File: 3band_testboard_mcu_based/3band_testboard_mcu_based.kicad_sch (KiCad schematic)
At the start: 0 parts

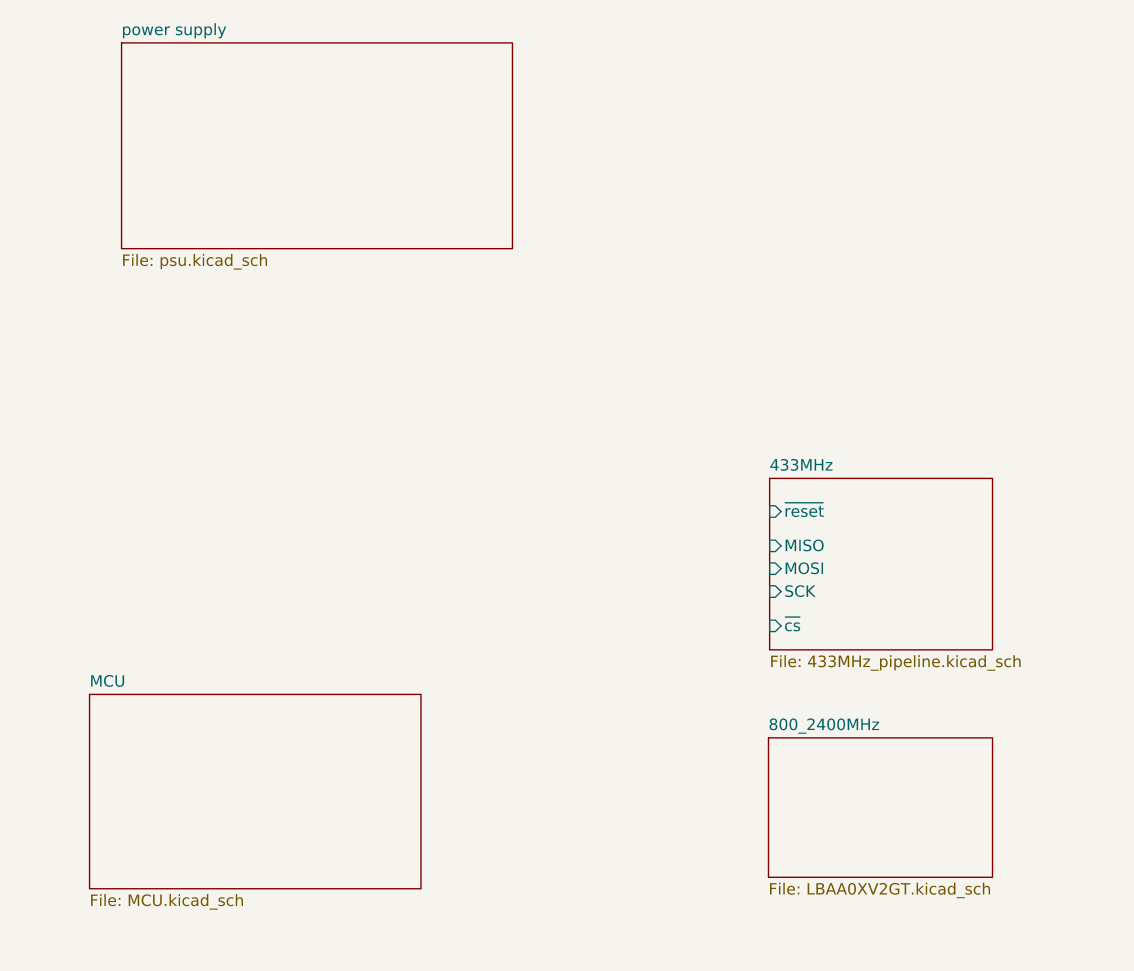
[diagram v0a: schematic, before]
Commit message: Færdiggjorde GPIO
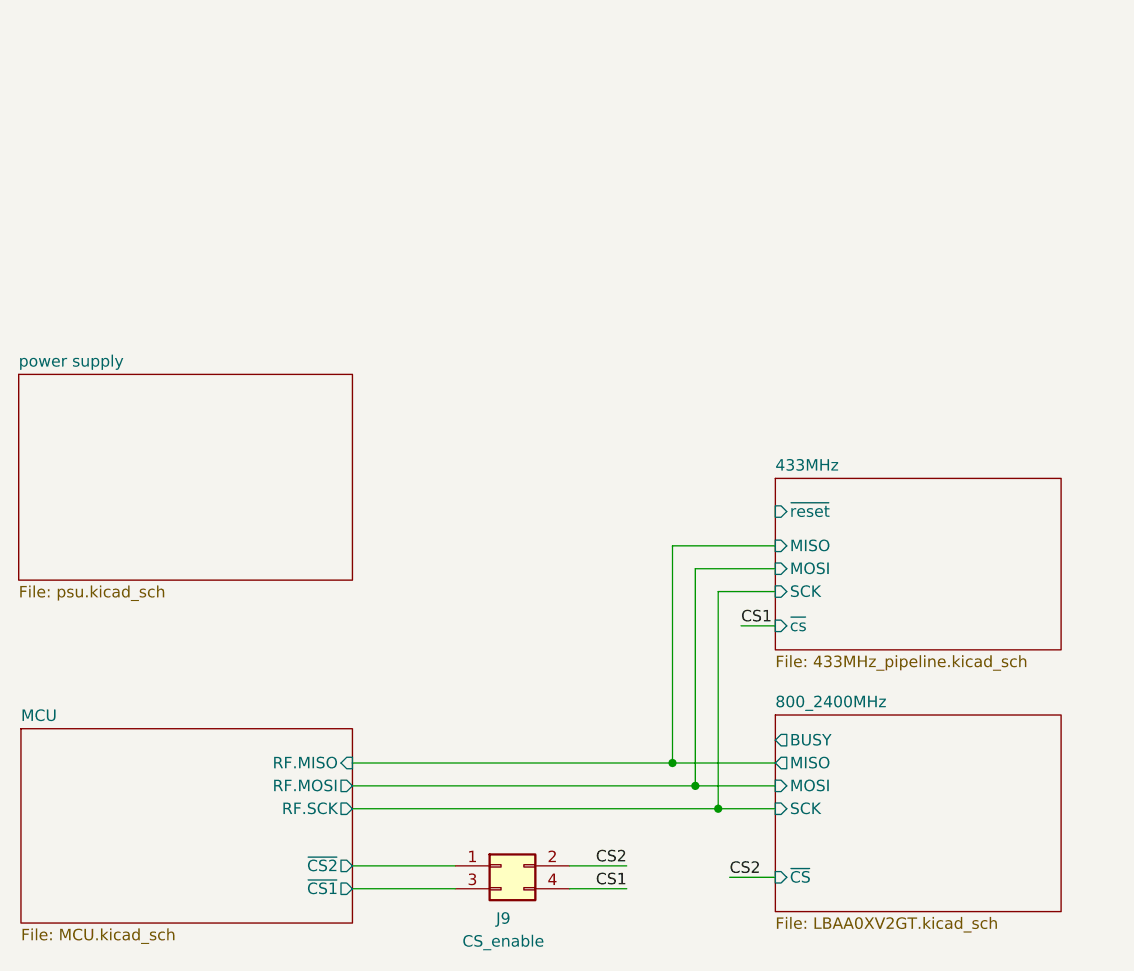
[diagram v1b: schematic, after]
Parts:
- added J9: CS_enable, Connector_PinHeader_2.54mm:PinHeader_2x02_P2.54mm_Vertical, symbol Connector_Generic:Conn_02x02_Odd_Even
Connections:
- new net CS1: J9.4 (Pin_4)
- new net CS2: J9.2 (Pin_2)
- new net MCU/~{CS1}: J9.3 (Pin_3)
- new net MCU/~{CS2}: J9.1 (Pin_1)
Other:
- sheet 800_2400MHz ports: added BUSY, MISO, MOSI, SCK, ~{CS}; removed none
- sheet MCU ports: added RF.MISO, RF.MOSI, RF.SCK, ~{CS1}, ~{CS2}; removed none
- company: (none) -> AAU-connectivity
- title: (none) -> 3-band-LoRa testboard

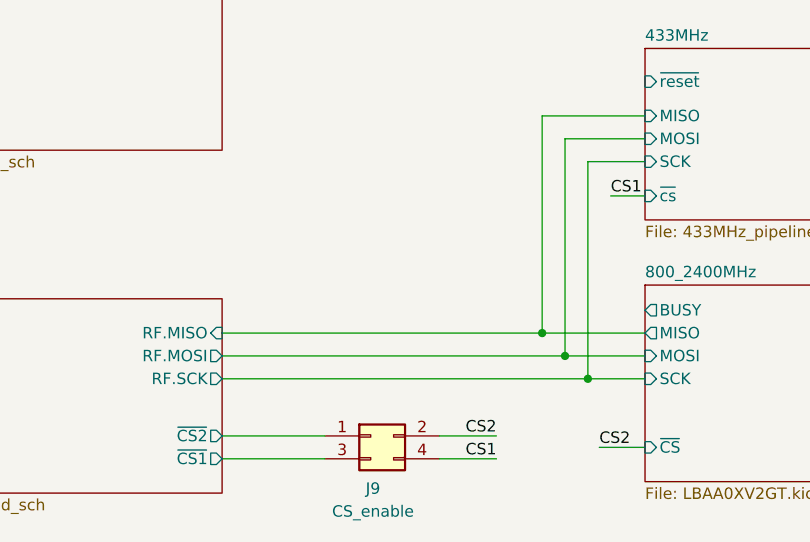
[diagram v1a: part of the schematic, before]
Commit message: DRC check, and price
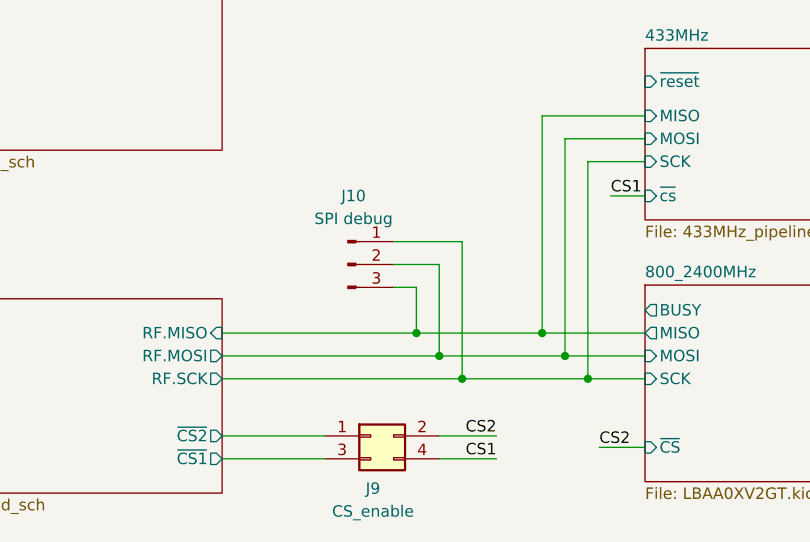
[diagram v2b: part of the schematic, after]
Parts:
- added J10: SPI debug, Connector_PinHeader_2.54mm:PinHeader_1x03_P2.54mm_Vertical, symbol Connector:Conn_01x03_Pin
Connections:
- net 433MHz/MISO: now also J10.3 (Pin_3)
- net 433MHz/MOSI: now also J10.2 (Pin_2)
- net 433MHz/SCK: now also J10.1 (Pin_1)
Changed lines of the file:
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@@
+	)
+	(junction
+		(at 123.19 104.14)
+		(diameter 0)
+		(color 0 0 0 0)
 	)
 	(junction
@@
 	)
 	(junction
+		(at 120.65 101.6)
+		(diameter 0)
+		(color 0 0 0 0)
+	)
+	(junction
+		(at 125.73 106.68)
+		(diameter 0)
+		(color 0 0 0 0)
+	)
+	(junction
 		(at 139.7 106.68)
 		(diameter 0)
@@
 	(wire
 		(pts
+			(xy 125.73 91.44) (xy 118.11 91.44)
+		)
+		(stroke
+			(width 0)
+			(type default)
+		)
+	)
+	(wire
+		(pts
 			(xy 123.19 115.57) (xy 129.54 115.57)
 		)
@@
 	(wire
 		(pts
+			(xy 123.19 104.14) (xy 123.19 93.98)
+		)
+		(stroke
+			(width 0)
+			(type default)
+		)
+	)
+	(wire
+		(pts
+			(xy 120.65 101.6) (xy 134.62 101.6)
+		)
+		(stroke
+			(width 0)
+			(type default)
+		)
+	)
+	(wire
+		(pts
 			(xy 137.16 104.14) (xy 146.05 104.14)
 		)
@@
 	(wire
 		(pts
-			(xy 99.06 101.6) (xy 134.62 101.6)
+			(xy 99.06 101.6) (xy 120.65 101.6)
 		)
 		(stroke
@@
 	(wire
 		(pts
+			(xy 125.73 106.68) (xy 139.7 106.68)
+		)
+		(stroke
+			(width 0)
+			(type default)
+		)
+	)
+	(wire
+		(pts
+			(xy 123.19 104.14) (xy 137.16 104.14)
+		)
+		(stroke
+			(width 0)
+			(type default)
+		)
+	)
+	(wire
+		(pts
 			(xy 99.06 115.57) (xy 110.49 115.57)
 		)
@@
 	(wire
 		(pts
-			(xy 99.06 106.68) (xy 139.7 106.68)
+			(xy 120.65 101.6) (xy 120.65 96.52)
+		)
+		(stroke
+			(width 0)
+			(type default)
+		)
+	)
+	(wire
+		(pts
+			(xy 99.06 106.68) (xy 125.73 106.68)
+		)
+		(stroke
+			(width 0)
+			(type default)
+		)
+	)
+	(wire
+		(pts
+			(xy 123.19 93.98) (xy 118.11 93.98)
 		)
 		(stroke
@@
 	(wire
 		(pts
-			(xy 99.06 104.14) (xy 137.16 104.14)
+			(xy 125.73 106.68) (xy 125.73 91.44)
+		)
+		(stroke
+			(width 0)
+			(type default)
+		)
+	)
+	(wire
+		(pts
+			(xy 99.06 104.14) (xy 123.19 104.14)
+		)
+		(stroke
+			(width 0)
+			(type default)
+		)
+	)
+	(wire
+		(pts
+			(xy 120.65 96.52) (xy 118.11 96.52)
 		)
 		(stroke
@@
 		)
 	)
+	(symbol
+		(lib_id "Connector:Conn_01x03_Pin")
+		(at 113.03 93.98 0)
+		(unit 1)
+		(exclude_from_sim no)
+		(in_bom yes)
+		(on_board yes)
+		(dnp no)
+		(fields_autoplaced yes)
+		(property "Reference" "J10"
+			(at 113.665 86.36 0)
+			(effects
+				(font
+					(size 1.27 1.27)
+				)
+			)
+		)
+		(property "Value" "SPI debug"
+			(at 113.665 88.9 0)
+			(effects
+				(font
+					(size 1.27 1.27)
+				)
+			)
+		)
+		(property "Footprint" "Connector_PinHeader_2.54mm:PinHeader_1x03_P2.54mm_Vertical"
+			(at 113.03 93.98 0)
+			(effects
+				(font
+					(size 1.27 1.27)
+				)
+				(hide yes)
+			)
+		)
+		(property "Datasheet" "~"
+			(at 113.03 93.98 0)
+			(effects
+				(font
+					(size 1.27 1.27)
+				)
+				(hide yes)
+			)
+		)
+		(property "Description" "Generic connector, single row, 01x03, script generated"
+			(at 113.03 93.98 0)
+			(effects
+				(font
+					(size 1.27 1.27)
+				)
+				(hide yes)
+			)
+		)
+		(pin "3"
+		)
+		(pin "1"
+		)
+		(pin "2"
+		)
+		(instances
+			(project ""
+				(path "/65994ec6-42d7-4e39-8f54-f3ae991c25e9"
+					(reference "J10")
+					(unit 1)
+				)
+			)
+		)
+	)
